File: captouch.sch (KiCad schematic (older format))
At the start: 39 parts, among them J401 MOLEX_502250-8037, J402 MOLEX_502250-8037, U401 FT5816LPC, X401 12MHz 18pF

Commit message: Schematic notes
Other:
- note added: "Optional CapTouch Interface"
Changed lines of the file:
@@
 Rev "v0.1"
 Comp ""
-Comment1 "Contains elements derived from Andrew \"Bunnie\" Huang \"LVDS to eDP adapter DVT1\""
+Comment1 ""
 Comment2 ""
 Comment3 "Creative Commons Attribution Sharealike License"
@@
 Wire Wire Line
 	7900 2150 7750 2150
+Text Notes 5800 850  0    157  ~ 0
+Optional CapTouch Interface
 $EndSCHEMATC

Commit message: Inductor choices
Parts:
- L401: value INDUCTOR -> BLM18KG121
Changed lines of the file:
@@
 P 1500 750
 F 0 "L401" H 1400 850 40  0000 C CNN
-F 1 "INDUCTOR" H 1500 700 40  0000 C CNN
+F 1 "BLM18KG121" H 1500 700 40  0000 C CNN
 F 2 "" H 1500 750 60  0000 C CNN
 F 3 "" H 1500 750 60  0000 C CNN

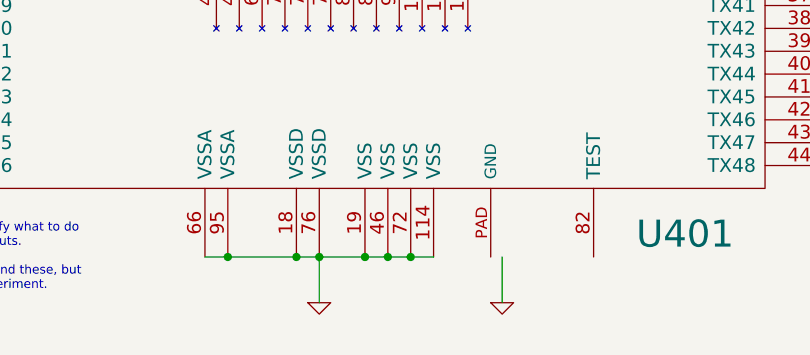
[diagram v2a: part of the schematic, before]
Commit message: Initial footprint association, last few footprints
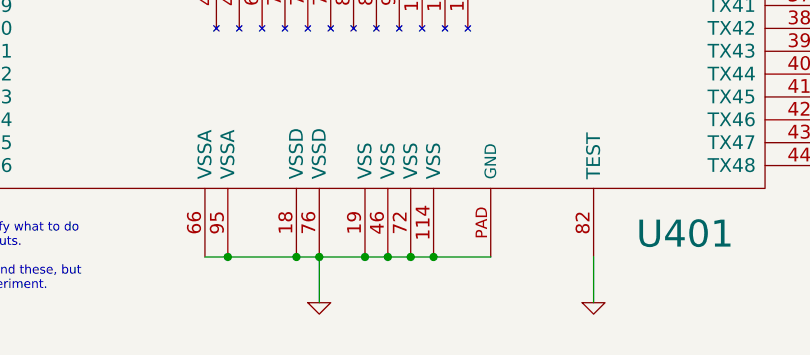
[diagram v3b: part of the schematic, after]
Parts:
- C401, C403, C404, C406, C407, C409: footprint (none) -> FT:1206
- C402: footprint (none) -> SMD_Packages:SMD-0402_c
- C405, C408, L401, R401, R402, R403, R404, R405, R406, R407, R408, R409: footprint (none) -> FT:0603
- J401, J402: footprint (none) -> novepad:MOLEX_502250_8037
- TP401, TP402, TP403, TP404, TP405, TP406, TP407, TP408, TP409, TP410, TP411, TP412, TP413, TP414, TP415, TP416: footprint (none) -> novepad:SMD_TEST_POINT
- U401: footprint (none) -> novepad:QFP40P1600X1600X100-129N
- X401: footprint (none) -> FT:HC49UP
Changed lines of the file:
@@
 LIBS:valves
 LIBS:novepad-cache
-EELAYER 24 0
+EELAYER 25 0
 EELAYER END
 $Descr A4 11693 8268
@@
 F 0 "R407" V 3330 1350 40  0000 C CNN
 F 1 "0R DNP" V 3257 1351 40  0000 C CNN
-F 2 "" V 3180 1350 30  0000 C CNN
+F 2 "FT:0603" V 3180 1350 30  0001 C CNN
 F 3 "" H 3250 1350 30  0000 C CNN
 	1    3250 1350
@@
 F 0 "R405" V 2230 1700 40  0000 C CNN
 F 1 "10K DNP" V 2157 1701 40  0000 C CNN
-F 2 "" V 2080 1700 30  0000 C CNN
+F 2 "FT:0603" V 2080 1700 30  0001 C CNN
 F 3 "" H 2150 1700 30  0000 C CNN
 	1    2150 1700
@@
 F 0 "R406" V 2630 1000 40  0000 C CNN
 F 1 "10K" V 2557 1001 40  0000 C CNN
-F 2 "" V 2480 1000 30  0000 C CNN
+F 2 "FT:0603" V 2480 1000 30  0001 C CNN
 F 3 "" H 2550 1000 30  0000 C CNN
 	1    2550 1000
@@
 F 0 "TP407" H 1630 2750 40  0000 L CNN
 F 1 "CONN_1" H 1550 2805 30  0001 C CNN
-F 2 "" H 1550 2750 60  0000 C CNN
+F 2 "novepad:SMD_TEST_POINT" H 1550 2750 60  0001 C CNN
 F 3 "" H 1550 2750 60  0000 C CNN
 	1    1550 2750
@@
 F 0 "TP405" H 1480 2850 40  0000 L CNN
 F 1 "CONN_1" H 1400 2905 30  0001 C CNN
-F 2 "" H 1400 2850 60  0000 C CNN
+F 2 "novepad:SMD_TEST_POINT" H 1400 2850 60  0001 C CNN
 F 3 "" H 1400 2850 60  0000 C CNN
 	1    1400 2850
@@
 F 0 "TP401" H 1330 2950 40  0000 L CNN
 F 1 "CONN_1" H 1250 3005 30  0001 C CNN
-F 2 "" H 1250 2950 60  0000 C CNN
+F 2 "novepad:SMD_TEST_POINT" H 1250 2950 60  0001 C CNN
 F 3 "" H 1250 2950 60  0000 C CNN
 	1    1250 2950
@@
 F 0 "R401" V 1080 3200 40  0000 C CNN
 F 1 "10K" V 1007 3201 40  0000 C CNN
-F 2 "" V 930 3200 30  0000 C CNN
+F 2 "FT:0603" V 930 3200 30  0001 C CNN
 F 3 "" H 1000 3200 30  0000 C CNN
 	1    1000 3200
@@
 L GND #PWR046
 U 1 1 5446F5C1
-P 4400 7500
-F 0 "#PWR046" H 4400 7500 30  0001 C CNN
-F 1 "GND" H 4400 7430 30  0001 C CNN
-F 2 "" H 4400 7500 60  0000 C CNN
-F 3 "" H 4400 7500 60  0000 C CNN
-	1    4400 7500
+P 4800 7500
+F 0 "#PWR046" H 4800 7500 30  0001 C CNN
+F 1 "GND" H 4800 7430 30  0001 C CNN
+F 2 "" H 4800 7500 60  0000 C CNN
+F 3 "" H 4800 7500 60  0000 C CNN
+	1    4800 7500
 	1    0    0    -1
 $EndComp
@@
 F 0 "X401" H 7450 1950 60  0000 C CNN
 F 1 "12MHz 18pF" H 7450 1650 60  0000 C CNN
-F 2 "" H 7450 1800 60  0000 C CNN
+F 2 "FT:HC49UP" H 7450 1800 60  0001 C CNN
 F 3 "" H 7450 1800 60  0000 C CNN
 	1    7450 1800
@@
 F 0 "C405" H 7050 2600 40  0000 L CNN
 F 1 "27pF" H 7056 2415 40  0000 L CNN
-F 2 "" H 7088 2350 30  0000 C CNN
+F 2 "FT:0603" H 7088 2350 30  0001 C CNN
 F 3 "" H 7050 2500 60  0000 C CNN
 	1    7050 2500
@@
 F 0 "C408" H 7900 2600 40  0000 L CNN
 F 1 "27pF" H 7906 2415 40  0000 L CNN
-F 2 "" H 7938 2350 30  0000 C CNN
+F 2 "FT:0603" H 7938 2350 30  0001 C CNN
 F 3 "" H 7900 2500 60  0000 C CNN
 	1    7900 2500
@@
 F 0 "C403" H 6600 3800 40  0000 L CNN
 F 1 "1uF 10V" H 6606 3615 40  0000 L CNN
-F 2 "" H 6638 3550 30  0000 C CNN
+F 2 "FT:1206" H 6638 3550 30  0001 C CNN
 F 3 "" H 6600 3700 60  0000 C CNN
 	1    6600 3700
@@
 F 0 "C407" H 7700 3800 40  0000 L CNN
 F 1 "1uF 10V" H 7706 3615 40  0000 L CNN
-F 2 "" H 7738 3550 30  0000 C CNN
+F 2 "FT:1206" H 7738 3550 30  0001 C CNN
 F 3 "" H 7700 3700 60  0000 C CNN
 	1    7700 3700
@@
 F 0 "R408" V 3930 1600 40  0000 C CNN
 F 1 "10R" V 3857 1601 40  0000 C CNN
-F 2 "" V 3780 1600 30  0000 C CNN
+F 2 "FT:0603" V 3780 1600 30  0001 C CNN
 F 3 "" H 3850 1600 30  0000 C CNN
 	1    3850 1600
@@
 F 0 "C406" H 7350 3800 40  0000 L CNN
 F 1 "1uF 10V" H 7356 3615 40  0000 L CNN
-F 2 "" H 7388 3550 30  0000 C CNN
+F 2 "FT:1206" H 7388 3550 30  0001 C CNN
 F 3 "" H 7350 3700 60  0000 C CNN
 	1    7350 3700
@@
 F 0 "C409" H 8100 3800 40  0000 L CNN
 F 1 "1uF 10V" H 8106 3615 40  0000 L CNN
-F 2 "" H 8138 3550 30  0000 C CNN
+F 2 "FT:1206" H 8138 3550 30  0001 C CNN
 F 3 "" H 8100 3700 60  0000 C CNN
 	1    8100 3700
@@
 F 0 "C404" H 6900 3800 40  0000 L CNN
 F 1 "1uF 10V" H 6906 3615 40  0000 L CNN
-F 2 "" H 6938 3550 30  0000 C CNN
+F 2 "FT:1206" H 6938 3550 30  0001 C CNN
 F 3 "" H 6900 3700 60  0000 C CNN
 	1    6900 3700
@@
 F 0 "C401" H 1850 1150 40  0000 L CNN
 F 1 "10uF 10V" H 1550 950 40  0000 L CNN
-F 2 "" H 1888 900 30  0000 C CNN
+F 2 "FT:1206" H 1888 900 30  0001 C CNN
 F 3 "" H 1850 1050 60  0000 C CNN
 	1    1850 1050
@@
 F 0 "C402" H 2150 1150 40  0000 L CNN
 F 1 "100nF 10V" H 2156 965 40  0000 L CNN
-F 2 "" H 2188 900 30  0000 C CNN
+F 2 "SMD_Packages:SMD-0402_c" H 2188 900 30  0001 C CNN
 F 3 "" H 2150 1050 60  0000 C CNN
 	1    2150 1050
@@
 F 0 "L401" H 1400 850 40  0000 C CNN
 F 1 "BLM18KG121" H 1500 700 40  0000 C CNN
-F 2 "" H 1500 750 60  0000 C CNN
+F 2 "FT:0603" H 1500 750 60  0001 C CNN
 F 3 "" H 1500 750 60  0000 C CNN
 	1    1500 750
@@
 F 0 "R403" V 1580 1450 40  0000 C CNN
 F 1 "22R" V 1507 1451 40  0000 C CNN
-F 2 "" V 1430 1450 30  0000 C CNN
+F 2 "FT:0603" V 1430 1450 30  0001 C CNN
 F 3 "" H 1500 1450 30  0000 C CNN
 	1    1500 1450
@@
 F 0 "R404" V 1580 1600 40  0000 C CNN
 F 1 "22R" V 1507 1601 40  0000 C CNN
-F 2 "" V 1430 1600 30  0000 C CNN
+F 2 "FT:0603" V 1430 1600 30  0001 C CNN
 F 3 "" H 1500 1600 30  0000 C CNN
 	1    1500 1600
@@
 F 0 "J401" H 9300 1850 60  0000 C CNN
 F 1 "MOLEX_502250-8037" H 9400 5700 60  0000 C CNN
-F 2 "" H 9200 2200 60  0000 C CNN
+F 2 "novepad:MOLEX_502250_8037" H 9200 2200 60  0001 C CNN
 F 3 "" H 9200 2200 60  0000 C CNN
 	1    9500 3800
@@
 F 0 "J402" H 10500 1850 60  0000 C CNN
 F 1 "MOLEX_502250-8037" H 10600 5700 60  0000 C CNN
-F 2 "" H 10400 2200 60  0000 C CNN
+F 2 "novepad:MOLEX_502250_8037" H 10400 2200 60  0001 C CNN
 F 3 "" H 10400 2200 60  0000 C CNN
 	1    10700 3800
@@
 	3600 7300 3600 7500
 Wire Wire Line
-	3100 7300 4100 7300
+	3100 7300 4350 7300
 Connection ~ 3600 7300
 Connection ~ 3500 7300
@@
 Connection ~ 4000 7300
 Wire Wire Line
-	4400 7300 4400 7500
+	4800 7300 4800 7500
 Wire Wire Line
 	5850 2200 6150 2200
@@
 F 0 "U401" H 5200 1900 118 0000 C CNN
 F 1 "FT5816LPC" H 3700 4650 157 0000 C CNN
-F 2 "" H 3600 5550 60  0000 C CNN
+F 2 "novepad:QFP40P1600X1600X100-129N" H 3600 5550 60  0001 C CNN
 F 3 "" H 3600 5550 60  0000 C CNN
 	1    3700 4550
@@
 F 0 "TP415" H 6380 6400 40  0000 L CNN
 F 1 "CONN_1" H 6300 6455 30  0001 C CNN
-F 2 "" H 6300 6400 60  0000 C CNN
+F 2 "novepad:SMD_TEST_POINT" H 6300 6400 60  0001 C CNN
 F 3 "" H 6300 6400 60  0000 C CNN
 	1    6300 6400
@@
 F 0 "R402" V 1480 7250 40  0000 C CNN
 F 1 "0R DNP" V 1407 7251 40  0000 C CNN
-F 2 "" V 1330 7250 30  0000 C CNN
+F 2 "FT:0603" V 1330 7250 30  0001 C CNN
 F 3 "" H 1400 7250 30  0000 C CNN
 	1    1400 7250
@@
 F 0 "TP406" H 1630 2250 40  0000 L CNN
 F 1 "CONN_1" H 1550 2305 30  0001 C CNN
-F 2 "" H 1550 2250 60  0000 C CNN
+F 2 "novepad:SMD_TEST_POINT" H 1550 2250 60  0001 C CNN
 F 3 "" H 1550 2250 60  0000 C CNN
 	1    1550 2250
@@
 F 0 "TP404" H 1480 2350 40  0000 L CNN
 F 1 "CONN_1" H 1400 2405 30  0001 C CNN
-F 2 "" H 1400 2350 60  0000 C CNN
+F 2 "novepad:SMD_TEST_POINT" H 1400 2350 60  0001 C CNN
 F 3 "" H 1400 2350 60  0000 C CNN
 	1    1400 2350
@@
 F 0 "TP409" H 4230 1450 40  0000 L CNN
 F 1 "CONN_1" H 4150 1505 30  0001 C CNN
-F 2 "" H 4150 1450 60  0000 C CNN
+F 2 "novepad:SMD_TEST_POINT" H 4150 1450 60  0001 C CNN
 F 3 "" H 4150 1450 60  0000 C CNN
 	1    4150 1450
@@
 F 0 "TP410" H 4780 1700 40  0000 L CNN
 F 1 "CONN_1" H 4700 1755 30  0001 C CNN
-F 2 "" H 4700 1700 60  0000 C CNN
+F 2 "novepad:SMD_TEST_POINT" H 4700 1700 60  0001 C CNN
 F 3 "" H 4700 1700 60  0000 C CNN
 	1    4700 1700
@@
 F 0 "TP411" H 5380 1700 40  0000 L CNN
 F 1 "CONN_1" H 5300 1755 30  0001 C CNN
-F 2 "" H 5300 1700 60  0000 C CNN
+F 2 "novepad:SMD_TEST_POINT" H 5300 1700 60  0001 C CNN
 F 3 "" H 5300 1700 60  0000 C CNN
 	1    5300 1700
@@
 F 0 "TP408" H 3480 1200 40  0000 L CNN
 F 1 "CONN_1" H 3400 1255 30  0001 C CNN
-F 2 "" H 3400 1200 60  0000 C CNN
+F 2 "novepad:SMD_TEST_POINT" H 3400 1200 60  0001 C CNN
 F 3 "" H 3400 1200 60  0000 C CNN
 	1    3400 1200
@@
 F 0 "TP414" H 6380 5600 40  0000 L CNN
 F 1 "CONN_1" H 6300 5655 30  0001 C CNN
-F 2 "" H 6300 5600 60  0000 C CNN
+F 2 "novepad:SMD_TEST_POINT" H 6300 5600 60  0001 C CNN
 F 3 "" H 6300 5600 60  0000 C CNN
 	1    6300 5600
@@
 F 0 "TP413" H 6380 5500 40  0000 L CNN
 F 1 "CONN_1" H 6300 5555 30  0001 C CNN
-F 2 "" H 6300 5500 60  0000 C CNN
+F 2 "novepad:SMD_TEST_POINT" H 6300 5500 60  0001 C CNN
 F 3 "" H 6300 5500 60  0000 C CNN
 	1    6300 5500
@@
 F 0 "TP402" H 1330 4000 40  0000 L CNN
 F 1 "CONN_1" H 1250 4055 30  0001 C CNN
-F 2 "" H 1250 4000 60  0000 C CNN
+F 2 "novepad:SMD_TEST_POINT" H 1250 4000 60  0001 C CNN
 F 3 "" H 1250 4000 60  0000 C CNN
 	1    1250 4000
@@
 F 0 "TP403" H 1330 4100 40  0000 L CNN
 F 1 "CONN_1" H 1250 4155 30  0001 C CNN
-F 2 "" H 1250 4100 60  0000 C CNN
+F 2 "novepad:SMD_TEST_POINT" H 1250 4100 60  0001 C CNN
 F 3 "" H 1250 4100 60  0000 C CNN
 	1    1250 4100
@@
 F 0 "TP412" H 6380 2300 40  0000 L CNN
 F 1 "CONN_1" H 6300 2355 30  0001 C CNN
-F 2 "" H 6300 2300 60  0000 C CNN
+F 2 "novepad:SMD_TEST_POINT" H 6300 2300 60  0001 C CNN
 F 3 "" H 6300 2300 60  0000 C CNN
 	1    6300 2300
@@
 F 0 "TP416" H 8980 2050 40  0000 L CNN
 F 1 "CONN_1" H 8900 2105 30  0001 C CNN
-F 2 "" H 8900 2050 60  0000 C CNN
+F 2 "novepad:SMD_TEST_POINT" H 8900 2050 60  0001 C CNN
 F 3 "" H 8900 2050 60  0000 C CNN
 	1    8900 2050
@@
 F 0 "R409" V 7580 2150 40  0000 C CNN
 F 1 "1M" V 7507 2151 40  0000 C CNN
-F 2 "" V 7430 2150 30  0000 C CNN
+F 2 "FT:0603" V 7430 2150 30  0001 C CNN
 F 3 "" H 7500 2150 30  0000 C CNN
 	1    7500 2150
@@
 Text Notes 5800 850  0    157  ~ 0
 Optional CapTouch Interface
+Connection ~ 4100 7300
 $EndSCHEMATC

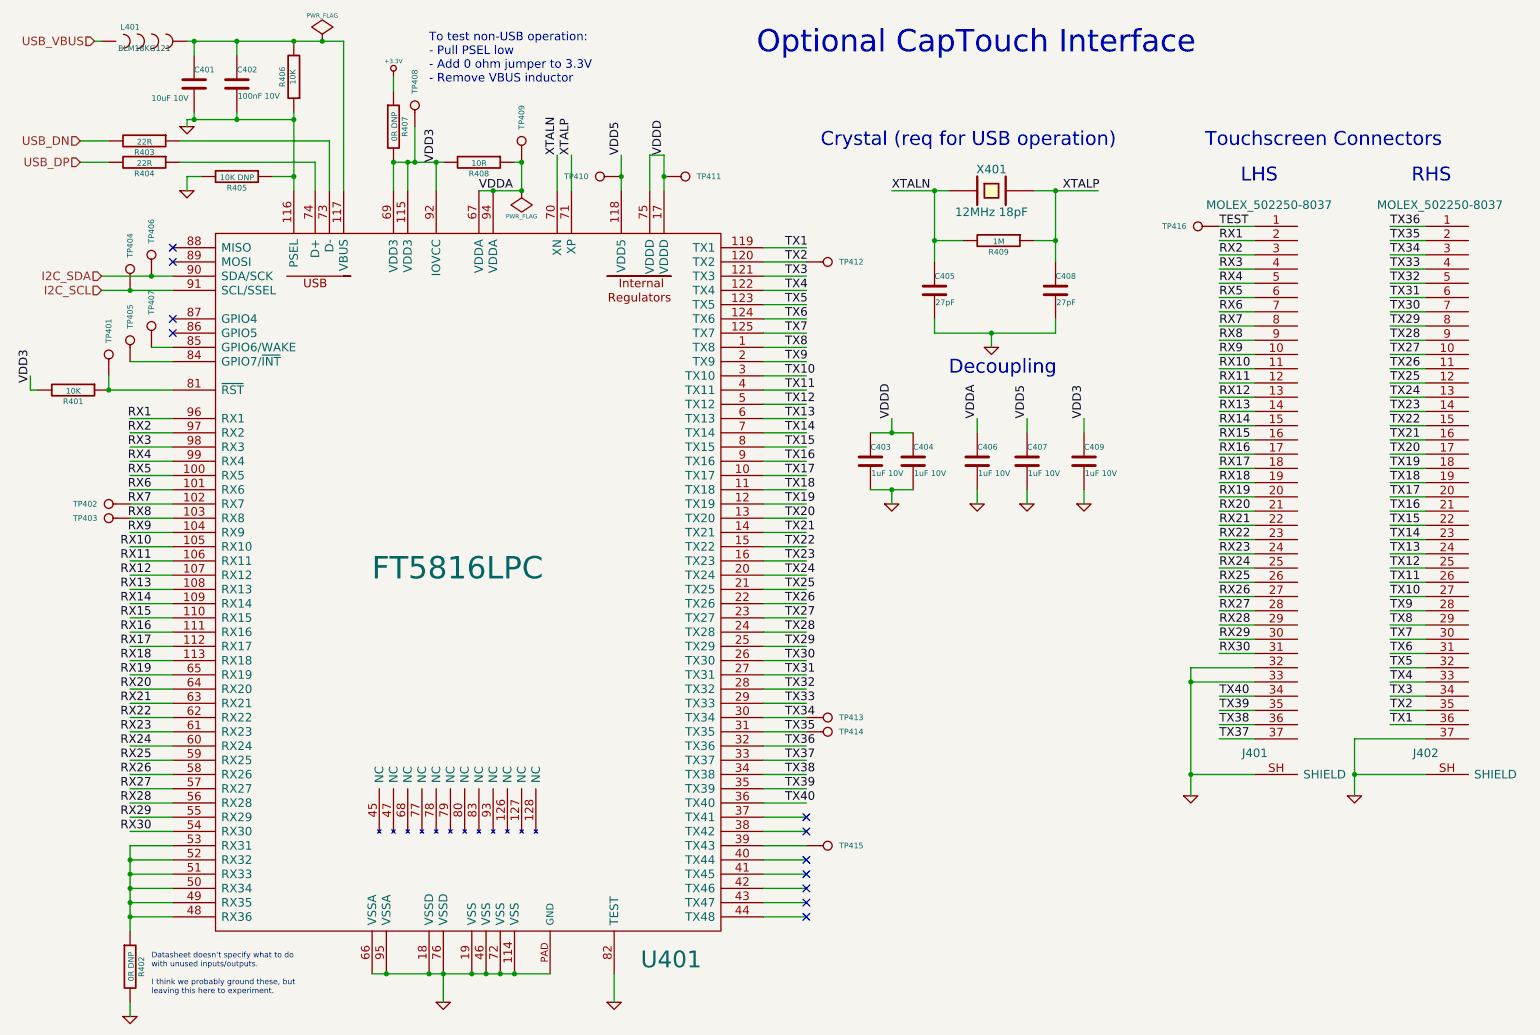
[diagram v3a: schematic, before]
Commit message: First attempt at routing the high speed differential traces
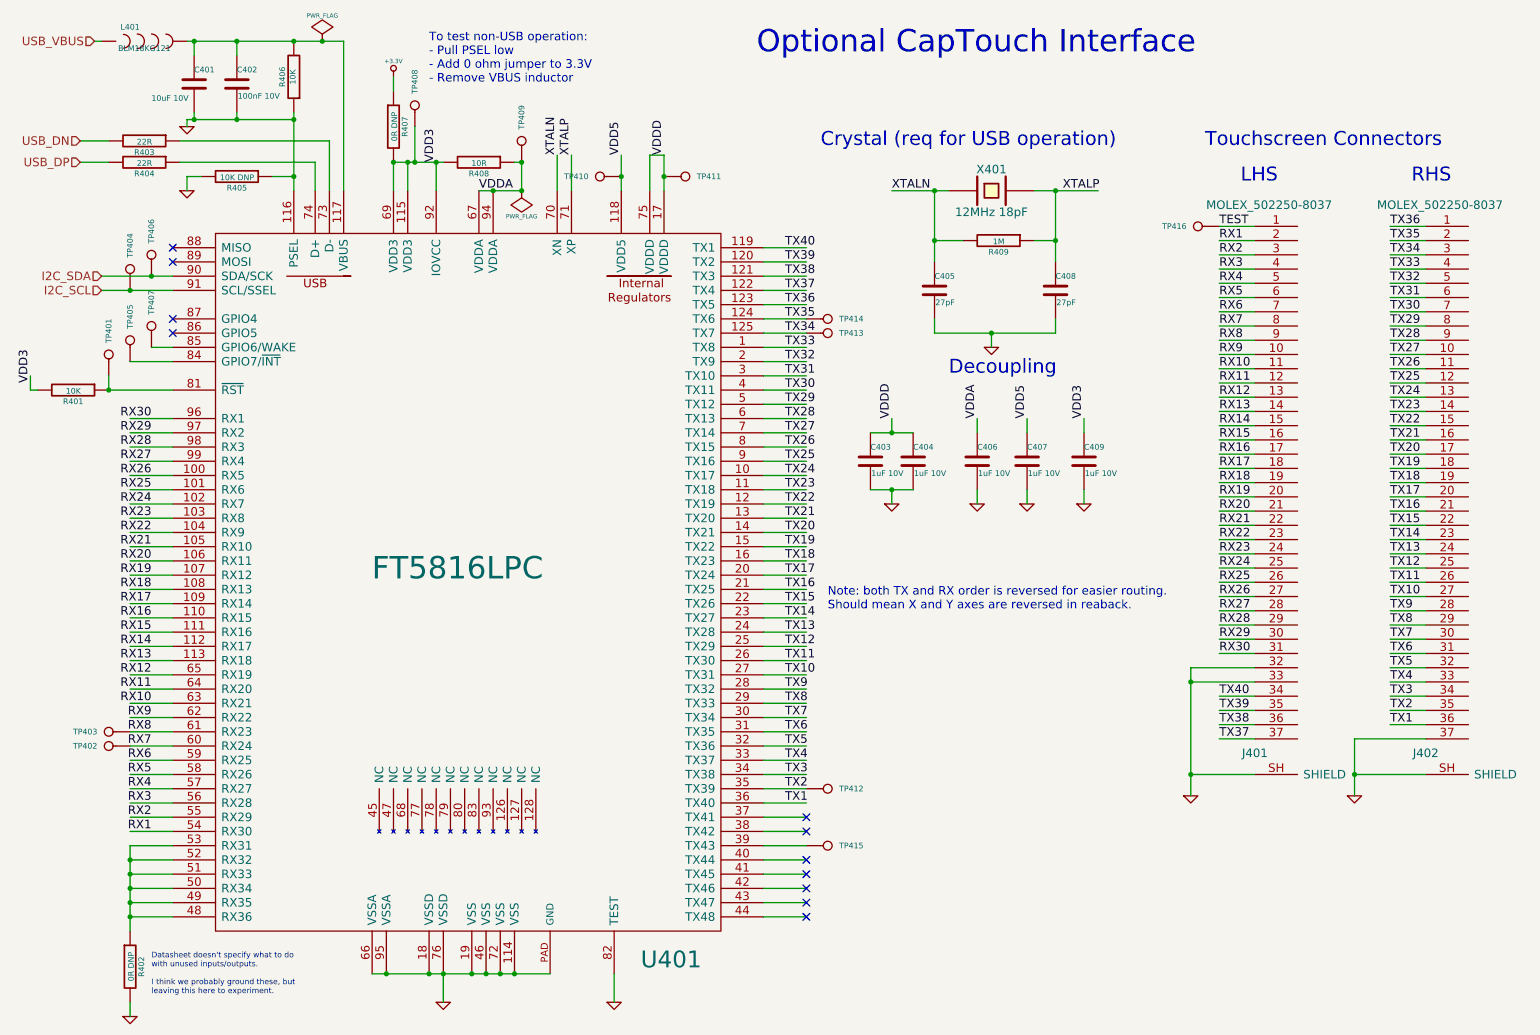
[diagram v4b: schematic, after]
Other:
- note added: "Note: both TX and RX order is reversed for easier routing.\nShould mean X and Y axes are reversed in reaback."
- moved on the sheet: TP402, TP403, TP412, TP413, TP414
